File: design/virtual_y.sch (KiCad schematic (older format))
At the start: 3 parts

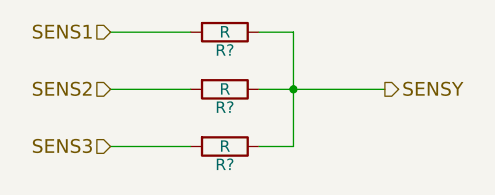
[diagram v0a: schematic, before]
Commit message: Assigned some footprints.
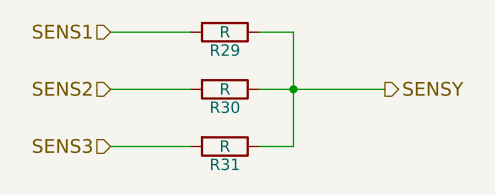
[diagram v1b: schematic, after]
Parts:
- gave numbers to parts that had none: 3
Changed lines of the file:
@@
 SENSY
 $Comp
-L R R?
+L R R29
 U 1 1 55E2B8A9
 P 4500 3100
-F 0 "R?" V 4580 3100 50  0000 C CNN
+F 0 "R29" V 4580 3100 50  0000 C CNN
 F 1 "R" V 4500 3100 50  0000 C CNN
-F 2 "" V 4430 3100 30  0000 C CNN
+F 2 "" V 4430 3100 30  0001 C CNN
 F 3 "" H 4500 3100 30  0000 C CNN
 	1    4500 3100
@@
 $EndComp
 $Comp
-L R R?
+L R R30
 U 1 1 55E2B8E8
 P 4500 3350
-F 0 "R?" V 4580 3350 50  0000 C CNN
+F 0 "R30" V 4580 3350 50  0000 C CNN
 F 1 "R" V 4500 3350 50  0000 C CNN
-F 2 "" V 4430 3350 30  0000 C CNN
+F 2 "" V 4430 3350 30  0001 C CNN
 F 3 "" H 4500 3350 30  0000 C CNN
 	1    4500 3350
@@
 $EndComp
 $Comp
-L R R?
+L R R31
 U 1 1 55E2B905
 P 4500 3600
-F 0 "R?" V 4580 3600 50  0000 C CNN
+F 0 "R31" V 4580 3600 50  0000 C CNN
 F 1 "R" V 4500 3600 50  0000 C CNN
-F 2 "" V 4430 3600 30  0000 C CNN
+F 2 "" V 4430 3600 30  0001 C CNN
 F 3 "" H 4500 3600 30  0000 C CNN
 	1    4500 3600

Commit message: Selected footprints
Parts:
- R29, R30, R31: footprint (none) -> Resistors_SMD:R_0603_HandSoldering
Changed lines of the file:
@@
 F 0 "R29" V 4580 3100 50  0000 C CNN
 F 1 "R" V 4500 3100 50  0000 C CNN
-F 2 "" V 4430 3100 30  0001 C CNN
+F 2 "Resistors_SMD:R_0603_HandSoldering" V 4430 3100 30  0001 C CNN
 F 3 "" H 4500 3100 30  0000 C CNN
 	1    4500 3100
@@
 F 0 "R30" V 4580 3350 50  0000 C CNN
 F 1 "R" V 4500 3350 50  0000 C CNN
-F 2 "" V 4430 3350 30  0001 C CNN
+F 2 "Resistors_SMD:R_0603_HandSoldering" V 4430 3350 30  0001 C CNN
 F 3 "" H 4500 3350 30  0000 C CNN
 	1    4500 3350
@@
 F 0 "R31" V 4580 3600 50  0000 C CNN
 F 1 "R" V 4500 3600 50  0000 C CNN
-F 2 "" V 4430 3600 30  0001 C CNN
+F 2 "Resistors_SMD:R_0603_HandSoldering" V 4430 3600 30  0001 C CNN
 F 3 "" H 4500 3600 30  0000 C CNN
 	1    4500 3600
